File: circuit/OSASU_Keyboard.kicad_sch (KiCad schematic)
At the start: 13 parts, among them J1 Conn_01x05_Pin, J2 Conn_01x05_Socket, J3 Conn_01x05_Pin, P1 USB_C_Plug_USB2.0, U1 CH552T, U2 CH32V003FxPx

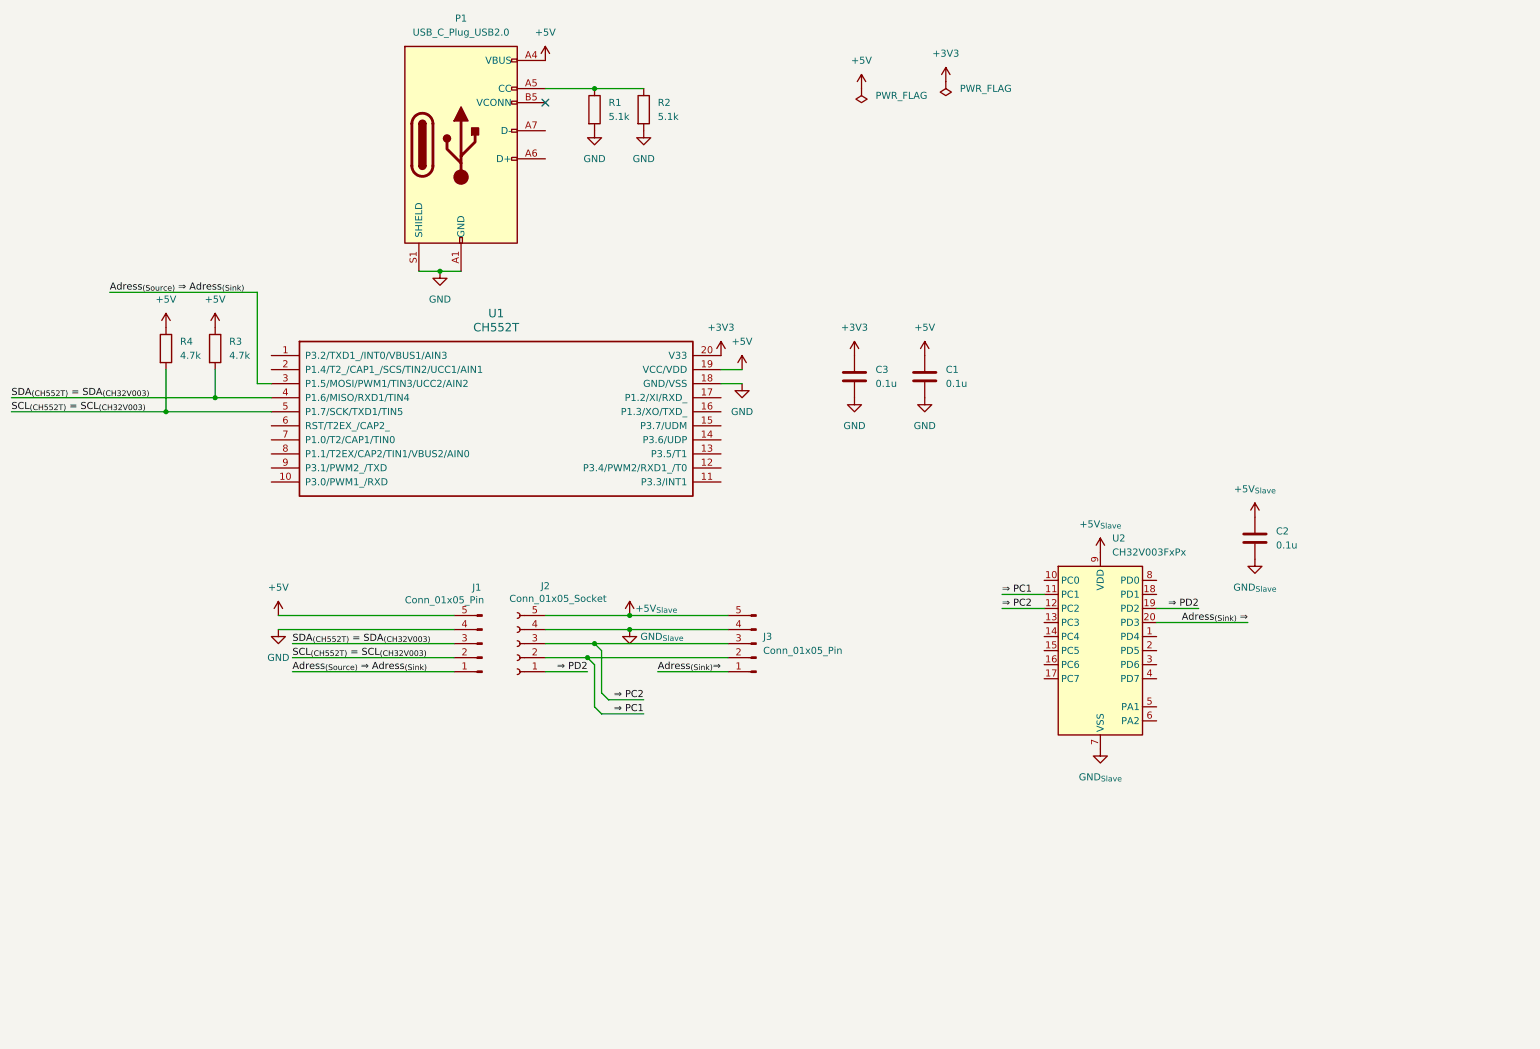
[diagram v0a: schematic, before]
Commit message: update schematic
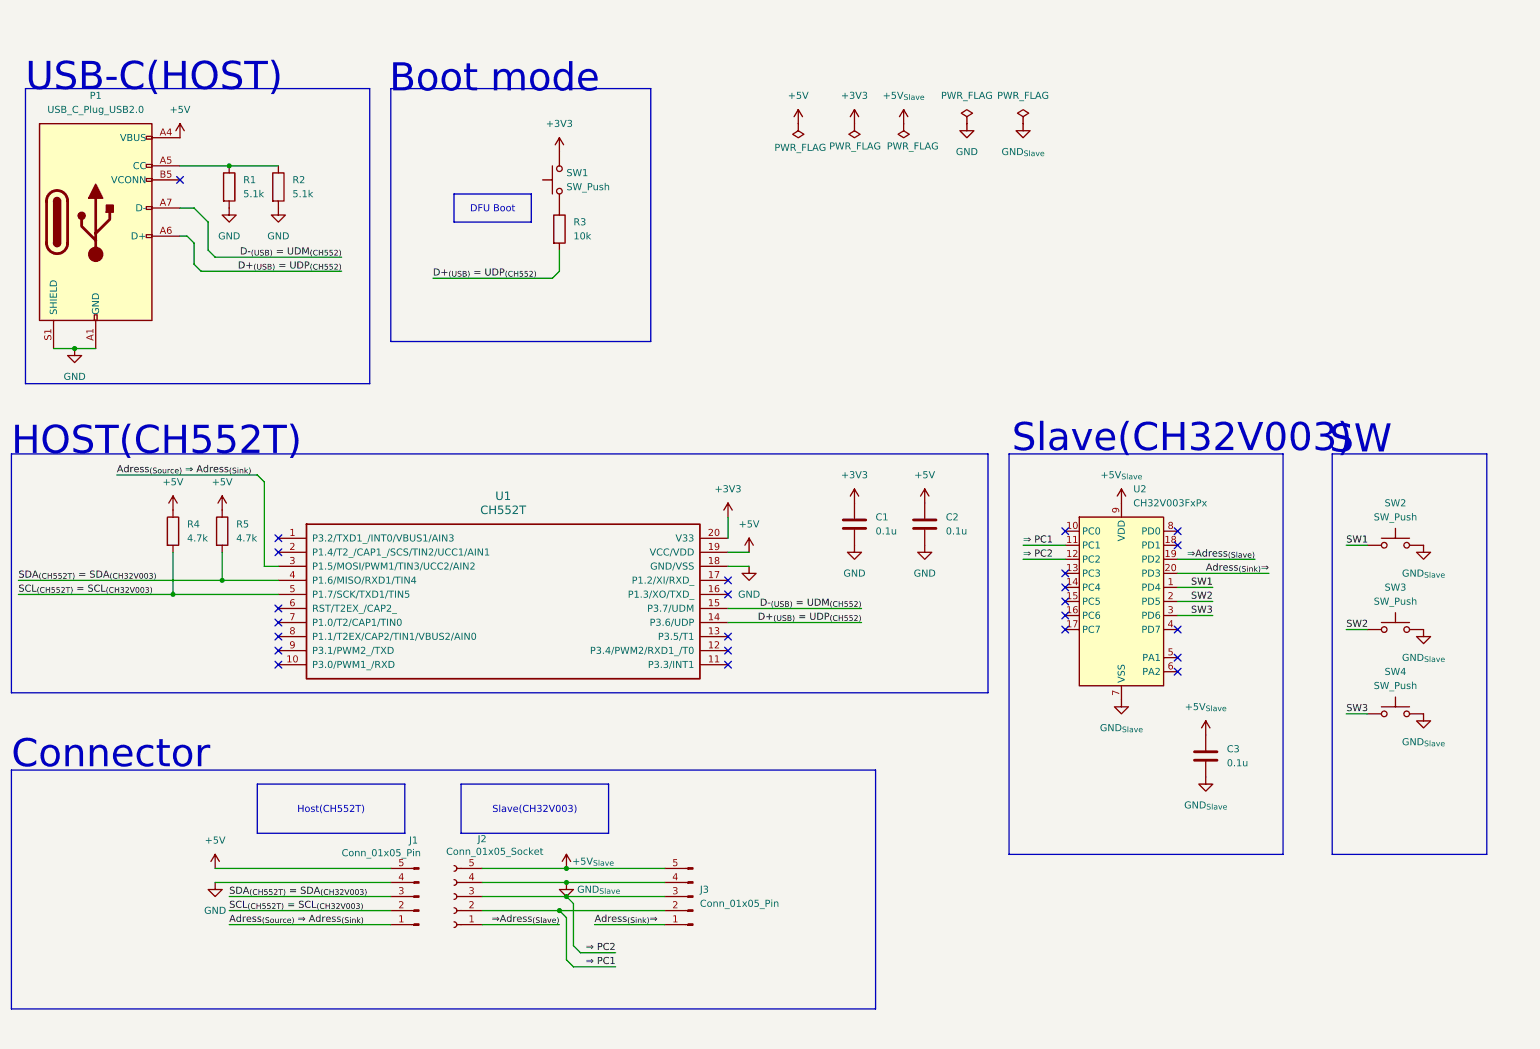
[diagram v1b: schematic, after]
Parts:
- added R3: 10k, symbol Device:R
- added SW1, SW2, SW3, SW4: SW_Push, symbol Switch:SW_Push
- renumbered C3 to C1, C1 to C2, C2 to C3, R3 to R5
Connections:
- net Adress_{(Sink)} ⇒  is gone; now on net Adress_{(Sink)}⇒ : U2.20 (PD3)
- net +3V3: now also SW1.2
- net GND_{Slave}: now also SW2.2, SW3.2, SW4.2
- net D+_{(USB)} = UDP_{(CH552)}: now reaches P1.A6 (D+)
- net D+_{(USB)} = UDP_{(CH552)}: now also U1.14 (P3.6/UDP), R3.2
- net D-_{(USB)} = UDM_{(CH552)}: now reaches P1.A7 (D-)
- net D-_{(USB)} = UDM_{(CH552)}: now also U1.15 (P3.7/UDM)
- net SW1: now reaches U2.1 (PD4)
- net SW1: now also SW2.1
- net SW2: now reaches U2.2 (PD5)
- net SW2: now also SW3.1
- net SW3: now reaches U2.3 (PD6)
- net SW3: now also SW4.1
- net ⇒ PD2 renamed ⇒Adress_{(Slave)}
- new net: R3.1, SW1.1
- no-connect marks 1 -> 24
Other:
- note added: "Boot mode"
- note added: "Connector"
- note added: "HOST(CH552T)"
- note added: "SW"
- note added: "Slave(CH32V003)"
- note added: "USB-C(HOST)"
- moved on the sheet: C1, C2, C3, J1, J2, J3, P1, R1, R2, R4, R5, U1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

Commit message: update schematic
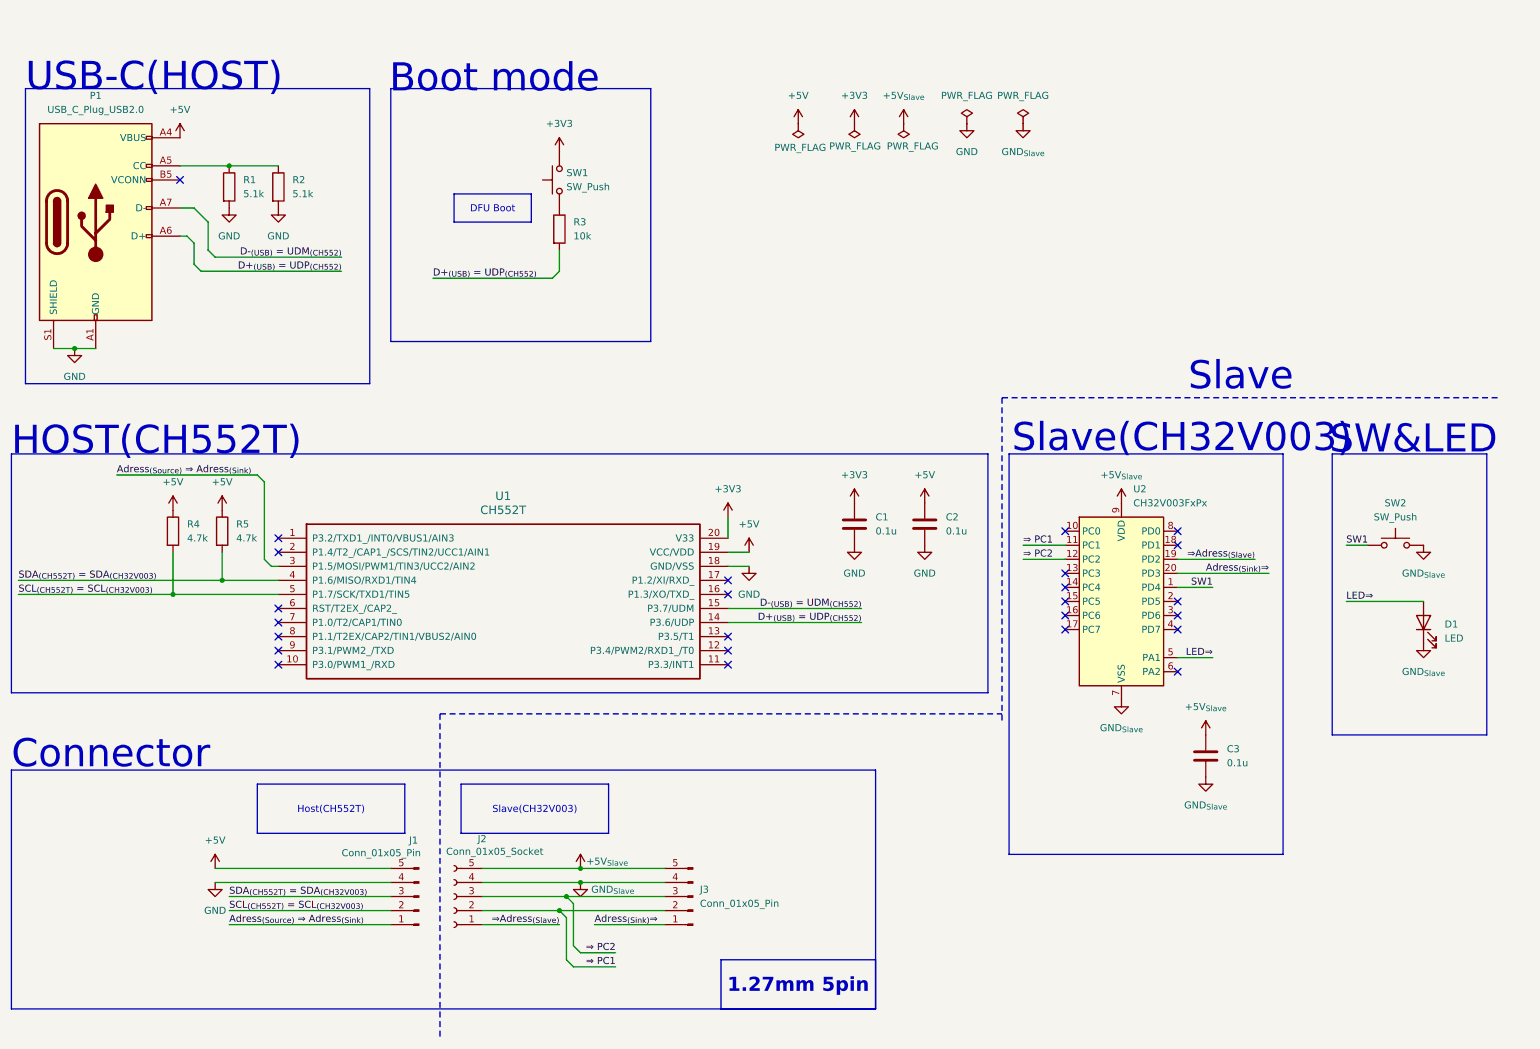
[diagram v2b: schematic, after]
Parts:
- removed SW3, SW4: SW_Push, symbol Switch:SW_Push
- added D1: LED, symbol Device:LED
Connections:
- net GND_{Slave}: now also D1.1 (K)
- net LED⇒ : now reaches U2.5 (PA1)
- net LED⇒ : now also D1.2 (A)
- net SW2: no longer names the net of U2.2 (PD5)
- net SW3: no longer names the net of U2.3 (PD6)
- no-connect marks 24 -> 25
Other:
- note added: "SW&LED"
- note added: "Slave"
- note removed: "SW"

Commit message: commit
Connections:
- net Adress_{(Sink)}⇒  renamed Adress_{(Sink)}⇒
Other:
- note removed: "Slave"
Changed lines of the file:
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@@
-		)
-	)
-	(text "Slave"
-		(exclude_from_sim no)
-		(at 237.49 77.47 0)
-		(effects
-			(font
-				(face "ＭＳ Ｐゴシック")
-				(size 5.08 5.08)
-			)
 		)
 	)
@@
 	(wire
 		(pts
-			(xy 226.06 110.49) (xy 240.03 110.49)
+			(xy 226.06 110.49) (xy 242.57 110.49)
 		)
 		(stroke
@@
 		)
 	)
-	(label "Adress_{(Sink)}⇒ "
+	(label "Adress_{(Sink)}⇒"
 		(at 242.57 113.03 180)
 		(effects
 			(font
+				(face "KiCad Font")
 				(size 1.27 1.27)
 				(color 0 0 0 1)
@@
 		(effects
 			(font
+				(face "KiCad Font")
 				(size 1.27 1.27)
 			)
@@
 		(effects
 			(font
+				(face "KiCad Font")
 				(size 1.27 1.27)
 			)
@@
 		(effects
 			(font
+				(face "KiCad Font")
 				(size 1.27 1.27)
 			)
@@
 		)
 	)
-	(label "Adress_{(Sink)}⇒ "
+	(label "Adress_{(Sink)}⇒"
 		(at 120.65 176.53 0)
 		(effects
 			(font
+				(face "KiCad Font")
 				(size 1.27 1.27)
 				(color 0 0 0 1)
@@
 	)
 	(label "⇒Adress_{(Slave)}"
-		(at 240.03 110.49 180)
-		(effects
-			(font
+		(at 242.57 110.49 180)
+		(effects
+			(font
+				(face "KiCad Font")
 				(size 1.27 1.27)
 			)
@@
 		(effects
 			(font
+				(face "KiCad Font")
 				(size 1.27 1.27)
 				(color 0 0 0 1)
@@
 		(effects
 			(font
+				(face "KiCad Font")
 				(size 1.27 1.27)
 			)
@@
 		(effects
 			(font
-				(size 1.27 1.27)
-			)
+				(face "KiCad Font")
+				(size 1.27 1.27)
+			)

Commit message: commit
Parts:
- C1, C2, C3: footprint (none) -> Capacitor_SMD:C_0603_1608Metric_Pad1.08x0.95mm_HandSolder
- D1: footprint (none) -> LED_THT:LED_D5.0mm
- J1, J2, J3: footprint (none) -> Connector_PinHeader_1.27mm:PinHeader_1x05_P1.27mm_Horizontal
- P1: footprint (none) -> Connector_USB:USB_C_Receptacle_GCT_USB4105-xx-A_16P_TopMnt_Horizontal
- R1, R2, R3, R4, R5: footprint (none) -> Resistor_SMD:R_0603_1608Metric_Pad0.98x0.95mm_HandSolder
- SW1, SW2: footprint (none) -> Button_Switch_Keyboard:SW_Cherry_MX_1.00u_PCB
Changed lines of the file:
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@@
 	(wire
 		(pts
+			(xy 50.8 48.26) (xy 50.8 54.61)
+		)
+		(stroke
+			(width 0)
+			(type default)
+		)
+	)
+	(wire
+		(pts
 			(xy 48.26 53.34) (xy 48.26 57.15)
 		)
@@
 	(wire
 		(pts
-			(xy 50.8 49.53) (xy 50.8 54.61)
+			(xy 26.67 72.39) (xy 30.48 72.39)
 		)
 		(stroke
@@
 	(wire
 		(pts
-			(xy 26.67 72.39) (xy 30.48 72.39)
+			(xy 53.34 109.22) (xy 53.34 114.3)
 		)
 		(stroke
@@
 	(wire
 		(pts
-			(xy 53.34 109.22) (xy 53.34 114.3)
+			(xy 242.57 113.03) (xy 226.06 113.03)
 		)
 		(stroke
@@
 	(wire
 		(pts
-			(xy 242.57 113.03) (xy 226.06 113.03)
+			(xy 52.07 55.88) (xy 74.93 55.88)
 		)
 		(stroke
@@
 	(wire
 		(pts
-			(xy 52.07 55.88) (xy 74.93 55.88)
+			(xy 118.11 166.37) (xy 133.35 166.37)
 		)
 		(stroke
@@
 	(wire
 		(pts
-			(xy 118.11 166.37) (xy 133.35 166.37)
+			(xy 168.91 121.92) (xy 144.78 121.92)
 		)
 		(stroke
@@
 	(wire
 		(pts
-			(xy 168.91 121.92) (xy 144.78 121.92)
+			(xy 118.11 181.61) (xy 124.46 181.61)
 		)
 		(stroke
@@
 	(wire
 		(pts
-			(xy 118.11 181.61) (xy 124.46 181.61)
+			(xy 49.53 46.99) (xy 50.8 48.26)
 		)
 		(stroke
@@
 	(wire
 		(pts
-			(xy 45.72 46.99) (xy 48.26 46.99)
+			(xy 45.72 46.99) (xy 49.53 46.99)
 		)
 		(stroke
@@
 	(wire
 		(pts
-			(xy 48.26 46.99) (xy 50.8 49.53)
-		)
-		(stroke
-			(width 0)
-			(type default)
-		)
-	)
-	(wire
-		(pts
 			(xy 114.3 173.99) (xy 133.35 173.99)
 		)
@@
 			)
 		)
-		(property "Footprint" ""
+		(property "Footprint" "Connector_USB:USB_C_Receptacle_GCT_USB4105-xx-A_16P_TopMnt_Horizontal"
 			(at 34.29 49.53 0)
 			(effects
@@
 			)
 		)
-		(property "Footprint" ""
+		(property "Footprint" "Capacitor_SMD:C_0603_1608Metric_Pad1.08x0.95mm_HandSolder"
 			(at 181.3052 107.95 0)
 			(effects
@@
 			)
 		)
-		(property "Footprint" ""
+		(property "Footprint" "Resistor_SMD:R_0603_1608Metric_Pad0.98x0.95mm_HandSolder"
 			(at 112.522 50.8 90)
 			(effects
@@
 			)
 		)
-		(property "Footprint" ""
+		(property "Footprint" "Capacitor_SMD:C_0603_1608Metric_Pad1.08x0.95mm_HandSolder"
 			(at 232.1052 149.86 0)
 			(effects
@@
 			)
 		)
-		(property "Footprint" ""
+		(property "Footprint" "Resistor_SMD:R_0603_1608Metric_Pad0.98x0.95mm_HandSolder"
 			(at 61.722 43.18 90)
 			(effects
@@
 			)
 		)
-		(property "Footprint" ""
+		(property "Footprint" "Resistor_SMD:R_0603_1608Metric_Pad0.98x0.95mm_HandSolder"
 			(at 52.832 43.18 90)
 			(effects
@@
 			)
 		)
-		(property "Footprint" ""
+		(property "Footprint" "Resistor_SMD:R_0603_1608Metric_Pad0.98x0.95mm_HandSolder"
 			(at 51.562 105.41 90)
 			(effects
@@
 			)
 		)
-		(property "Footprint" ""
+		(property "Footprint" "Resistor_SMD:R_0603_1608Metric_Pad0.98x0.95mm_HandSolder"
 			(at 42.672 105.41 90)
 			(effects
@@
 			)
 		)
-		(property "Footprint" ""
+		(property "Footprint" "Connector_PinHeader_1.27mm:PinHeader_1x05_P1.27mm_Horizontal"
 			(at 88.9 171.45 0)
 			(effects
@@
 			)
 		)
-		(property "Footprint" ""
+		(property "Footprint" "Capacitor_SMD:C_0603_1608Metric_Pad1.08x0.95mm_HandSolder"
 			(at 168.6052 107.95 0)
 			(effects
@@
 			)
 		)
-		(property "Footprint" ""
+		(property "Footprint" "Button_Switch_Keyboard:SW_Cherry_MX_1.00u_PCB"
 			(at 265.43 102.87 0)
 			(effects
@@
 			)
 		)
-		(property "Footprint" ""
+		(property "Footprint" "Connector_PinHeader_1.27mm:PinHeader_1x05_P1.27mm_Horizontal"
 			(at 95.25 171.45 0)
 			(effects
@@
 			)
 		)
-		(property "Footprint" ""
+		(property "Footprint" "Connector_PinHeader_1.27mm:PinHeader_1x05_P1.27mm_Horizontal"
 			(at 138.43 171.45 0)
 			(effects
@@
 			)
 		)
-		(property "Footprint" ""
+		(property "Footprint" "LED_THT:LED_D5.0mm"
 			(at 270.51 121.92 0)
 			(effects
@@
 			)
 		)
-		(property "Footprint" ""
+		(property "Footprint" "Button_Switch_Keyboard:SW_Cherry_MX_1.00u_PCB"
 			(at 109.22 41.91 0)
 			(effects

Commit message: commit
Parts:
- removed SW1: SW_Push, Button_Switch_Keyboard:SW_Cherry_MX_1.00u_PCB, symbol Switch:SW_Push
- added JP1: Jumper_2_Open, Jumper:SolderJumper-2_P1.3mm_Open_RoundedPad1.0x1.5mm, symbol Jumper:Jumper_2_Open
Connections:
- net +3V3: now also JP1.2 (B)
- net at R3.1: now also JP1.1 (A)
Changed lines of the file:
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@@
+	)
+	(symbol
+		(lib_id "Jumper:Jumper_2_Open")
+		(at 114.3 41.91 90)
+		(unit 1)
+		(exclude_from_sim no)
+		(in_bom yes)
+		(on_board yes)
+		(dnp no)
+		(fields_autoplaced yes)
+		(property "Reference" "JP1"
+			(at 115.57 40.6399 90)
+			(effects
+				(font
+					(size 1.27 1.27)
+				)
+				(justify right)
+			)
+		)
+		(property "Value" "Jumper_2_Open"
+			(at 115.57 43.1799 90)
+			(effects
+				(font
+					(size 1.27 1.27)
+				)
+				(justify right)
+			)
+		)
+		(property "Footprint" "Jumper:SolderJumper-2_P1.3mm_Open_RoundedPad1.0x1.5mm"
+			(at 114.3 41.91 0)
+			(effects
+				(font
+					(size 1.27 1.27)
+				)
+				(hide yes)
+			)
+		)
+		(property "Datasheet" "~"
+			(at 114.3 41.91 0)
+			(effects
+				(font
+					(size 1.27 1.27)
+				)
+				(hide yes)
+			)
+		)
+		(property "Description" "Jumper, 2-pole, open"
+			(at 114.3 41.91 0)
+			(effects
+				(font
+					(size 1.27 1.27)
+				)
+				(hide yes)
+			)
+		)
+		(pin "2"
+		)
+		(pin "1"
+		)
+		(instances
+			(project ""
+				(path "/84df409d-4a1b-4f85-a3c2-89dbdb50c821"
+					(reference "JP1")
+					(unit 1)
+				)
+			)
+		)
 	)
 	(symbol
@@
 					(unit 1)
 				)
-			)
-		)
-	)
-	(symbol
-		(lib_id "Switch:SW_Push")
-		(at 114.3 41.91 90)
-		(unit 1)
-		(exclude_from_sim no)
-		(in_bom yes)
-		(on_board yes)
-		(dnp no)
-		(fields_autoplaced yes)
-		(property "Reference" "SW1"
-			(at 115.57 40.6399 90)
-			(effects
-				(font
-					(size 1.27 1.27)
-				)
-				(justify right)
-			)
-		)
-		(property "Value" "SW_Push"
-			(at 115.57 43.1799 90)
-			(effects
-				(font
-					(size 1.27 1.27)
-				)
-				(justify right)
-			)
-		)
-		(property "Footprint" "Button_Switch_Keyboard:SW_Cherry_MX_1.00u_PCB"
-			(at 109.22 41.91 0)
-			(effects
-				(font
-					(size 1.27 1.27)
-				)
-				(hide yes)
-			)
-		)
-		(property "Datasheet" "~"
-			(at 109.22 41.91 0)
-			(effects
-				(font
-					(size 1.27 1.27)
-				)
-				(hide yes)
-			)
-		)
-		(property "Description" "Push button switch, generic, two pins"
-			(at 114.3 41.91 0)
-			(effects
-				(font
-					(size 1.27 1.27)
-				)
-				(hide yes)
-			)
-		)
-		(pin "1"
-		)
-		(pin "2"
-		)
-		(instances
-			(project ""
-				(path "/84df409d-4a1b-4f85-a3c2-89dbdb50c821"
-					(reference "SW1")
-					(unit 1)
-				)

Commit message: commit
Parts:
- D1: footprint LED_THT:LED_D5.0mm -> LED_SMD:LED_Yuji_5730
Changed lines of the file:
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@@
 			)
 		)
-		(property "Footprint" "LED_THT:LED_D5.0mm"
+		(property "Footprint" "LED_SMD:LED_Yuji_5730"
 			(at 270.51 121.92 0)
 			(effects

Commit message: commit
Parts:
- J3: footprint Connector_PinHeader_1.27mm:PinHeader_1x05_P1.27mm_Horizontal -> custom:PinHeader_1x05_P2.54mm_Right_angle
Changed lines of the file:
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@@
 			)
 		)
-		(property "Footprint" "Connector_PinHeader_1.27mm:PinHeader_1x05_P1.27mm_Horizontal"
+		(property "Footprint" "custom:PinHeader_1x05_P2.54mm_Right_angle"
 			(at 138.43 171.45 0)
 			(effects

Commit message: schematicを更新
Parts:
- removed C1, C2, C3: 0.1u, Capacitor_SMD:C_0603_1608Metric_Pad1.08x0.95mm_HandSolder, symbol Device:C
- removed D1: LED, LED_SMD:LED_Yuji_5730, symbol Device:LED
- removed JP1: Jumper_2_Open, Jumper:SolderJumper-2_P1.3mm_Open_RoundedPad1.0x1.5mm, symbol Jumper:Jumper_2_Open
- removed P1: USB_C_Plug_USB2.0, Connector_USB:USB_C_Receptacle_GCT_USB4105-xx-A_16P_TopMnt_Horizontal, symbol Connector:USB_C_Plug_USB2.0
- removed R1, R2: 5.1k, Resistor_SMD:R_0603_1608Metric_Pad0.98x0.95mm_HandSolder, symbol Device:R
- removed R3: 10k, Resistor_SMD:R_0603_1608Metric_Pad0.98x0.95mm_HandSolder, symbol Device:R
- removed R4, R5: 4.7k, Resistor_SMD:R_0603_1608Metric_Pad0.98x0.95mm_HandSolder, symbol Device:R
- removed SW2: SW_Push, Button_Switch_Keyboard:SW_Cherry_MX_1.00u_PCB, symbol Switch:SW_Push
- removed U1: CH552T, Package_SO:TSSOP-20_4.4x6.5mm_P0.65mm, symbol wch:CH552T
- removed U2: CH32V003FxPx, Package_SO:TSSOP-20_4.4x6.5mm_P0.65mm, symbol MCU_WCH_CH32V0:CH32V003FxPx
- added J4: Conn_01x05_Socket, Connector_PinHeader_1.27mm:PinHeader_1x05_P1.27mm_Horizontal, symbol Connector:Conn_01x05_Socket
- added J5: Conn_01x05_Pin, custom:PinHeader_1x05_P2.54mm_Right_angle, symbol Connector:Conn_01x05_Pin
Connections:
- net +5V renamed HOST/+5V
- net +5V_{Slave} renamed Sleve/+5V_{Slave}
- net Adress_{(Sink)}⇒ renamed Sleve/Adress(Sink)
- net Adress_{(Source)} ⇒ Adress_{(Sink)} renamed HOST/Adress
- net GND renamed HOST/GND
- net GND_{Slave} renamed Sleve/GND_{Slave}
- net SCL_{(CH552T)} = SCL_{(CH32V003)} renamed HOST/SDA
- net SDA_{(CH552T)} = SDA_{(CH32V003)} renamed HOST/SCL
- net ⇒ PC1 renamed Sleve/PC2
- net ⇒ PC2 renamed Sleve/PC1
- net ⇒Adress_{(Slave)} renamed Sleve/Adress(Slave)
- new net: J4.1 (Pin_1), J5.1 (Pin_1)
- new net: J4.2 (Pin_2), J5.2 (Pin_2)
- new net: J4.3 (Pin_3), J5.3 (Pin_3)
- new net: J4.4 (Pin_4), J5.4 (Pin_4)
- new net: J4.5 (Pin_5), J5.5 (Pin_5)
- no-connect marks 25 -> 0
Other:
- added sheet HOST (host.kicad_sch)
- added sheet Sleve (sleve.kicad_sch)
- note removed: "Boot mode"
- note removed: "Connector"
- note removed: "HOST(CH552T)"
- note removed: "SW&LED"
- note removed: "Slave(CH32V003)"
- note removed: "USB-C(HOST)"
